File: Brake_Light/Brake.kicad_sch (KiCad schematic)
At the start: 76 parts, among them J1 Conn_01x03, J10 Conn_01x08, J11 Conn_01x08, J13 Conn_01x08, J14 Conn_01x08, J15 Conn_01x08, J16 Conn_01x08, J17 Conn_01x08, J2 Brake, J3 Conn_01x05, J4 Conn_01x05, J9 Conn_01x08, SW1 SW_SPST, SW2 SW_SPST, U1 STM32F103C8Tx, U2 SN65HVD256D, U4 AP2204K-ADJ, U5 AP63200WU, U6 MAX7219CNG+, U7 MAX7219CNG+, U8 MAX7219CNG+, U9 MAX7219CNG+, Y1 8M, Y2 32.768k

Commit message: feat : BrakeLight layout
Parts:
- removed H1, H2, H3, H4: MountingHole_Pad, MountingHole:MountingHole_3.2mm_M3_ISO14580_Pad, symbol Mechanical:MountingHole_Pad
- removed J2: Brake, Connector_JST:JST_XH_B2B-XH-A_1x02_P2.50mm_Vertical, symbol Connector_Generic:Conn_01x02
- U6, U7, U8, U9: value MAX7219CNG+ -> MAX7219CNG
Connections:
- net Brake renamed BSPD_IN
- no-connect marks 25 -> 26

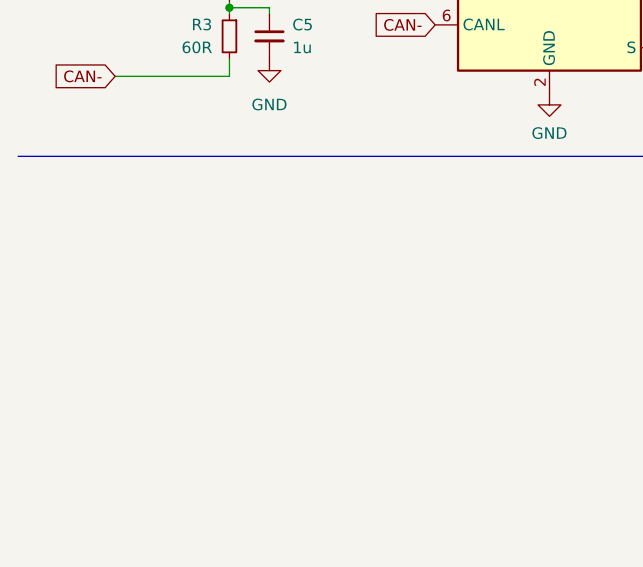
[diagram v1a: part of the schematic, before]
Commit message: fix: mounting hole
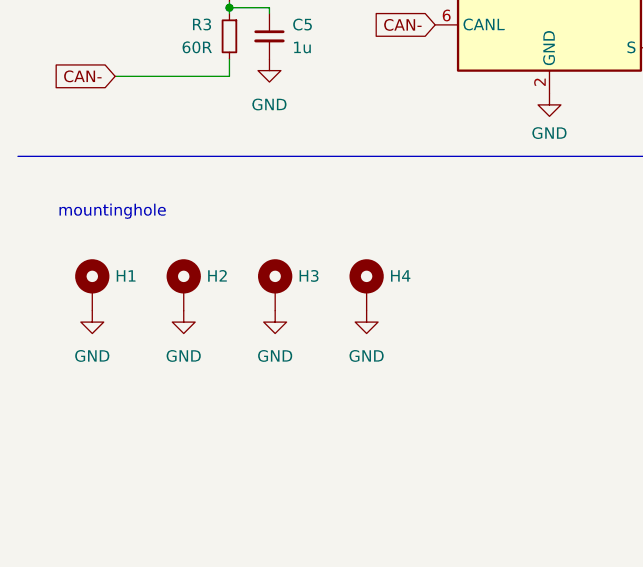
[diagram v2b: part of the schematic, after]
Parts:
- added H1, H2, H3, H4: MountingHole_Pad, MountingHole:MountingHole_3.2mm_M3_ISO7380_Pad, symbol Mechanical:MountingHole_Pad
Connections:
- net GND: now also H1.1, H2.1, H3.1, H4.1
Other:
- note added: "mountinghole"
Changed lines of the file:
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@@
     (effects (font (size 5 5) (thickness 2) bold) (justify left bottom))
   )
+  (text "mountinghole" (at 15.875 238.76 0)
+    (effects (font (size 1.27 1.27)) (justify left bottom))
+  )
   (text "DCDC\n" (at 172.085 55.88 0)
     (effects (font (size 5 5) (thickness 1) bold) (justify left bottom))
@@
     )
   )
+  (symbol (lib_id "Mechanical:MountingHole_Pad") (at 29.845 246.38 0) (unit 1)
+    (in_bom yes) (on_board yes) (dnp no) (fields_autoplaced)
+    (property "Reference" "H2" (at 32.385 245.11 0)
+      (effects (font (size 1.27 1.27)) (justify left))
+    )
+    (property "Value" "MountingHole_Pad" (at 32.385 246.38 0)
+      (effects (font (size 1.27 1.27)) (justify left) hide)
+    )
+    (property "Footprint" "MountingHole:MountingHole_3.2mm_M3_ISO7380_Pad" (at 29.845 246.38 0)
+      (effects (font (size 1.27 1.27)) hide)
+    )
+    (property "Datasheet" "~" (at 29.845 246.38 0)
+      (effects (font (size 1.27 1.27)) hide)
+    )
+    (pin "1")
+    (instances
+      (project "Brake"
+        (path "/8e33e74c-19fc-43ec-a25a-6f96812462e5"
+          (reference "H2") (unit 1)
+        )
+      )
+    )
+  )
   (symbol (lib_id "power:+3V3") (at 72.39 23.495 0) (unit 1)
     (in_bom yes) (on_board yes) (dnp no) (fields_autoplaced)
@@
     )
   )
+  (symbol (lib_id "Mechanical:MountingHole_Pad") (at 19.685 246.38 0) (unit 1)
+    (in_bom yes) (on_board yes) (dnp no) (fields_autoplaced)
+    (property "Reference" "H1" (at 22.225 245.11 0)
+      (effects (font (size 1.27 1.27)) (justify left))
+    )
+    (property "Value" "MountingHole_Pad" (at 22.225 246.38 0)
+      (effects (font (size 1.27 1.27)) (justify left) hide)
+    )
+    (property "Footprint" "MountingHole:MountingHole_3.2mm_M3_ISO7380_Pad" (at 19.685 246.38 0)
+      (effects (font (size 1.27 1.27)) hide)
+    )
+    (property "Datasheet" "~" (at 19.685 246.38 0)
+      (effects (font (size 1.27 1.27)) hide)
+    )
+    (pin "1")
+    (instances
+      (project "Brake"
+        (path "/8e33e74c-19fc-43ec-a25a-6f96812462e5"
+          (reference "H1") (unit 1)
+        )
+      )
+    )
+  )
   (symbol (lib_id "power:GND") (at 17.78 31.115 0) (unit 1)
     (in_bom yes) (on_board yes) (dnp no)
@@
     )
   )
+  (symbol (lib_id "Mechanical:MountingHole_Pad") (at 40.005 246.38 0) (unit 1)
+    (in_bom yes) (on_board yes) (dnp no)
+    (property "Reference" "H3" (at 42.545 245.11 0)
+      (effects (font (size 1.27 1.27)) (justify left))
+    )
+    (property "Value" "MountingHole_Pad" (at 42.545 246.38 0)
+      (effects (font (size 1.27 1.27)) (justify left) hide)
+    )
+    (property "Footprint" "MountingHole:MountingHole_3.2mm_M3_ISO7380_Pad" (at 40.005 246.38 0)
+      (effects (font (size 1.27 1.27)) hide)
+    )
+    (property "Datasheet" "~" (at 40.005 246.38 0)
+      (effects (font (size 1.27 1.27)) hide)
+    )
+    (pin "1")
+    (instances
+      (project "Brake"
+        (path "/8e33e74c-19fc-43ec-a25a-6f96812462e5"
+          (reference "H3") (unit 1)
+        )
+      )
+    )
+  )
   (symbol (lib_id "power:GND") (at 158.115 170.815 0) (unit 1)
     (in_bom yes) (on_board yes) (dnp no) (fields_autoplaced)
@@
     )
   )
+  (symbol (lib_id "power:GND") (at 29.845 248.92 0) (unit 1)
+    (in_bom yes) (on_board yes) (dnp no) (fields_autoplaced)
+    (property "Reference" "#PWR014" (at 29.845 255.27 0)
+      (effects (font (size 1.27 1.27)) hide)
+    )
+    (property "Value" "GND" (at 29.845 254 0)
+      (effects (font (size 1.27 1.27)))
+    )
+    (property "Footprint" "" (at 29.845 248.92 0)
+      (effects (font (size 1.27 1.27)) hide)
+    )
+    (property "Datasheet" "" (at 29.845 248.92 0)
+      (effects (font (size 1.27 1.27)) hide)
+    )
+    (pin "1")
+    (instances
+      (project "Brake"
+        (path "/8e33e74c-19fc-43ec-a25a-6f96812462e5"
+          (reference "#PWR014") (unit 1)
+        )
+      )
+    )
+  )
   (symbol (lib_id "power:GND") (at 143.51 214.63 270) (unit 1)
     (in_bom yes) (on_board yes) (dnp no) (fields_autoplaced)
@@
     )
   )
+  (symbol (lib_id "power:GND") (at 40.005 248.92 0) (unit 1)
+    (in_bom yes) (on_board yes) (dnp no) (fields_autoplaced)
+    (property "Reference" "#PWR015" (at 40.005 255.27 0)
+      (effects (font (size 1.27 1.27)) hide)
+    )
+    (property "Value" "GND" (at 40.005 254 0)
+      (effects (font (size 1.27 1.27)))
+    )
+    (property "Footprint" "" (at 40.005 248.92 0)
+      (effects (font (size 1.27 1.27)) hide)
+    )
+    (property "Datasheet" "" (at 40.005 248.92 0)
+      (effects (font (size 1.27 1.27)) hide)
+    )
+    (pin "1")
+    (instances
+      (project "Brake"
+        (path "/8e33e74c-19fc-43ec-a25a-6f96812462e5"
+          (reference "#PWR015") (unit 1)
+        )
+      )
+    )
+  )
   (symbol (lib_id "Device:C") (at 278.765 34.29 0) (unit 1)
     (in_bom yes) (on_board yes) (dnp no)
@@
     )
   )
+  (symbol (lib_id "power:GND") (at 50.165 248.92 0) (unit 1)
+    (in_bom yes) (on_board yes) (dnp no) (fields_autoplaced)
+    (property "Reference" "#PWR016" (at 50.165 255.27 0)
+      (effects (font (size 1.27 1.27)) hide)
+    )
+    (property "Value" "GND" (at 50.165 254 0)
+      (effects (font (size 1.27 1.27)))
+    )
+    (property "Footprint" "" (at 50.165 248.92 0)
+      (effects (font (size 1.27 1.27)) hide)
+    )
+    (property "Datasheet" "" (at 50.165 248.92 0)
+      (effects (font (size 1.27 1.27)) hide)
+    )
+    (pin "1")
+    (instances
+      (project "Brake"
+        (path "/8e33e74c-19fc-43ec-a25a-6f96812462e5"
+          (reference "#PWR016") (unit 1)
+        )
+      )
+    )
+  )
   (symbol (lib_id "Device:C_Small") (at 194.31 31.75 0) (unit 1)
     (in_bom yes) (on_board yes) (dnp no)
@@
     )
   )
+  (symbol (lib_id "Mechanical:MountingHole_Pad") (at 50.165 246.38 0) (unit 1)
+    (in_bom yes) (on_board yes) (dnp no)
+    (property "Reference" "H4" (at 52.705 245.11 0)
+      (effects (font (size 1.27 1.27)) (justify left))
+    )
+    (property "Value" "MountingHole_Pad" (at 52.705 246.38 0)
+      (effects (font (size 1.27 1.27)) (justify left) hide)
+    )
+    (property "Footprint" "MountingHole:MountingHole_3.2mm_M3_ISO7380_Pad" (at 50.165 246.38 0)
+      (effects (font (size 1.27 1.27)) hide)
+    )
+    (property "Datasheet" "~" (at 50.165 246.38 0)
+      (effects (font (size 1.27 1.27)) hide)
+    )
+    (pin "1")
+    (instances
+      (project "Brake"
+        (path "/8e33e74c-19fc-43ec-a25a-6f96812462e5"
+          (reference "H4") (unit 1)
+        )
+      )
+    )
+  )
   (symbol (lib_id "power:GND") (at 308.61 140.97 0) (unit 1)
     (in_bom yes) (on_board yes) (dnp no) (fields_autoplaced)
@@
         )
       )
+    )
+  )
+  (symbol (lib_id "power:GND") (at 19.685 248.92 0) (unit 1)
+    (in_bom yes) (on_board yes) (dnp no) (fields_autoplaced)
+    (property "Reference" "#PWR013" (at 19.685 255.27 0)
+      (effects (font (size 1.27 1.27)) hide)
+    )
+    (property "Value" "GND" (at 19.685 254 0)
+      (effects (font (size 1.27 1.27)))
+    )
+    (property "Footprint" "" (at 19.685 248.92 0)
+      (effects (font (size 1.27 1.27)) hide)
+    )
+    (property "Datasheet" "" (at 19.685 248.92 0)
+      (effects (font (size 1.27 1.27)) hide)
+    )
+    (pin "1")
+    (instances
+      (project "Brake"
+        (path "/8e33e74c-19fc-43ec-a25a-6f96812462e5"
+          (reference "#PWR013") (unit 1)
+        )
+      )
